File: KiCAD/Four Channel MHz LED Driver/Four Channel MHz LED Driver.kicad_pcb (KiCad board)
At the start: 2 copper layers, 100 x 100 mm, 92 parts, among them J1 Barrel_Jack_Switch, J10 Conn_01x24_Female, J2 Conn_01x02_Female, J3 8P8C_Shielded_x4, J4 Conn_01x03_Male, J5 Conn_01x03_Female, J6 Conn_01x08_Female, J7 Conn_01x03_Female, J8 Conn_01x05_Female, J9 Conn_01x24_Female, M1 Fan_4pin, Q1 SUM70060E, SW1 Pushbutton_with_LED, SW2 Pushbutton_with_LED, SW3 Pushbutton_with_LED, SW4 Pushbutton_with_LED, SW5 SW_SPDT, U1 12V boost, U10 ASSR-1218, U11 ASSR-1218, U12 Teensy3.6, U2 SN74LV4T125PWR, U3 DPBW06F-05, U4 TMUX1204DGSR, U5 BDJ0GA5WEFJ-E2, U6 ADP7182AUJZ-1.8-R7, U7 LT6200CS8-10, U8 ASSR-1218, U9 ASSR-1218

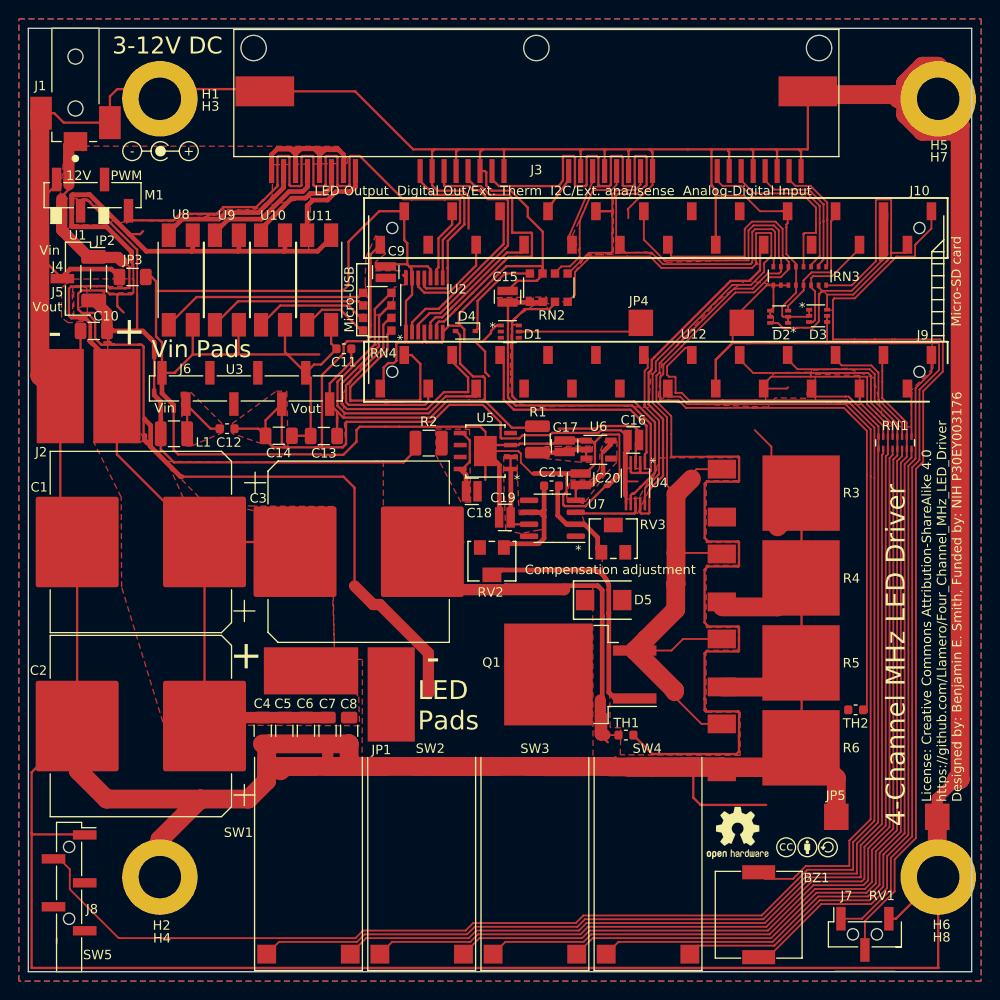
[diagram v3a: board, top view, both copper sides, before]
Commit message: Fix 4.7kx8 footprint
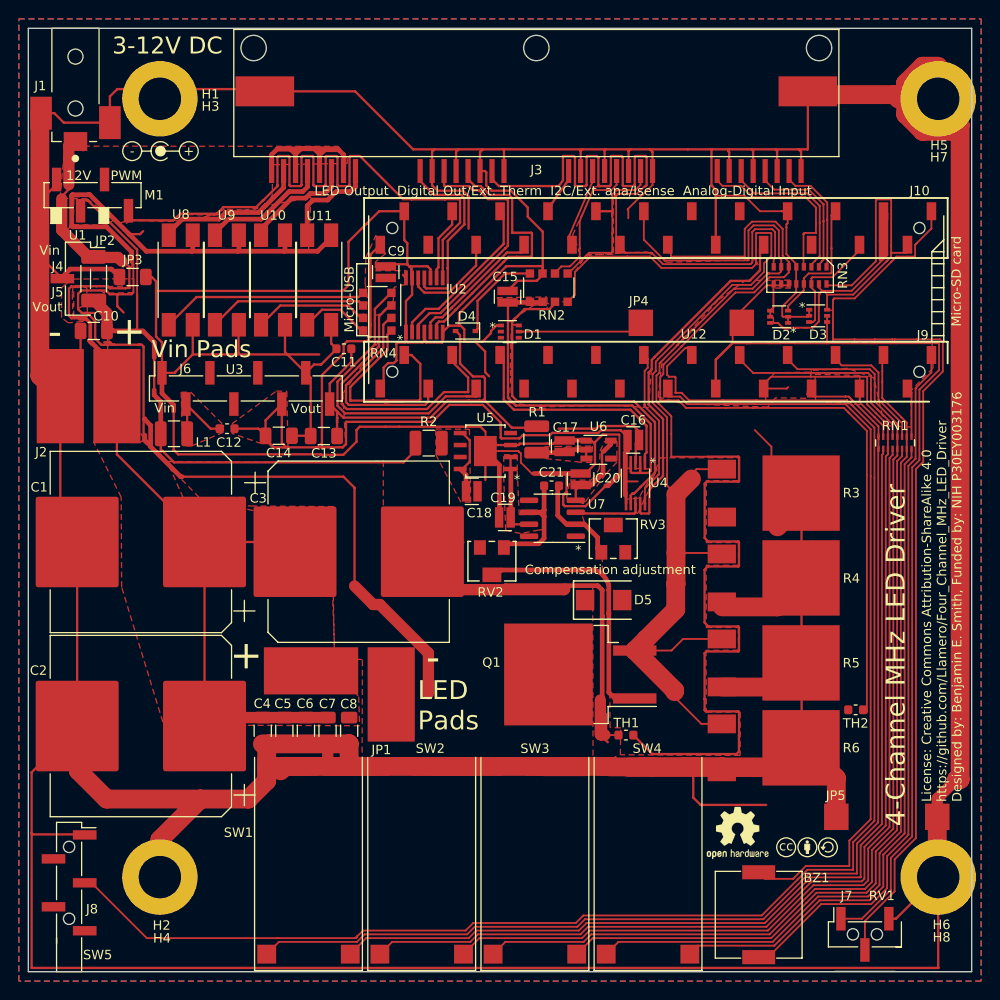
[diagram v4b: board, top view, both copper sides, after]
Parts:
- RN3: footprint Custom Footprints:2506_8x_R-pack -> Custom Footprints:2506_modified_concave_8x_R-pack
- moved R1 0.08 mm to (90.9, 67.6)
- moved RN3 0.07 mm to (118.8, 50.2), turned to 180 degrees
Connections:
- SW5 pad 2: /Toggle_switch -> GND
- SW5 pad 3: Net-(SW5-Pad3) -> /Toggle_switch
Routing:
- net /Toggle_switch: track 170.6 -> 166.0 mm
- net /A-D_input_1: track 13.8 -> 14.9 mm

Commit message: Schematic check
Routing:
- net /Isense: track 117.8 -> 124.5 mm

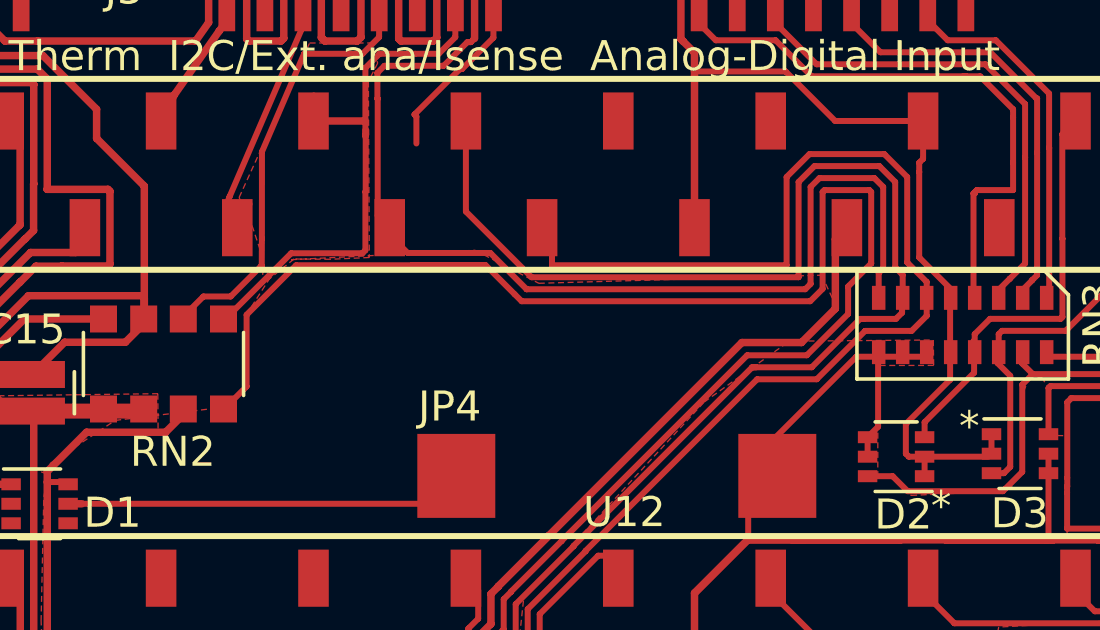
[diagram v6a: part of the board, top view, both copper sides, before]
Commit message: Fix back silkscreen lines
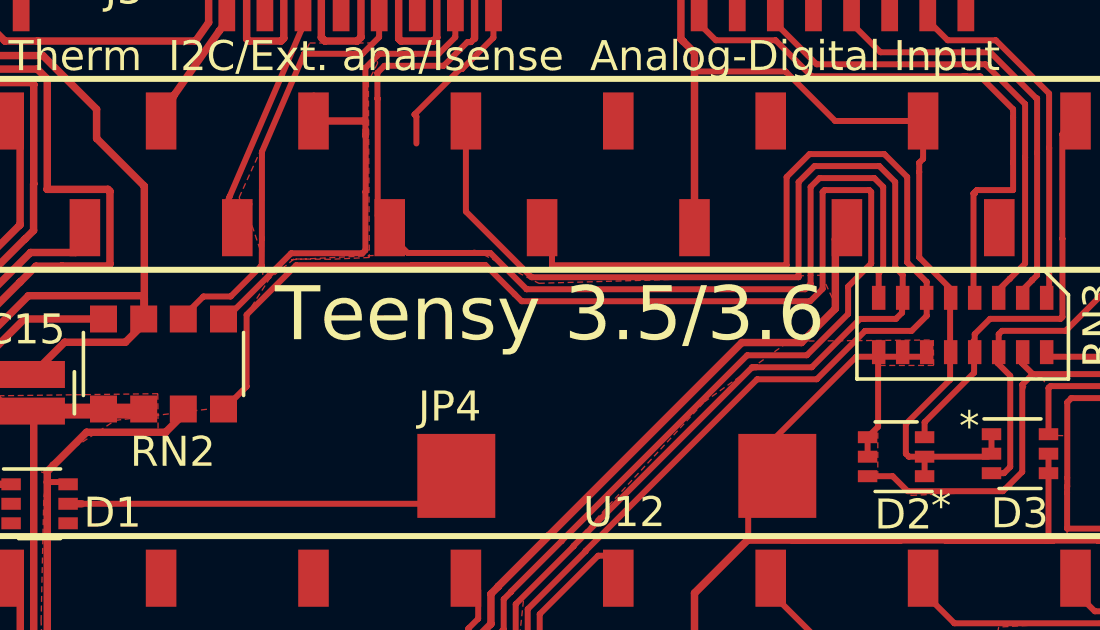
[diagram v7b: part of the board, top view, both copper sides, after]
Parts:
- RN4: value R_Pack04 -> 200
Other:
- board text added: "Teensy 3.5/3.6"
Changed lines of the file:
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@@
   (general
     (thickness 1.6)
-    (drawings 18)
+    (drawings 19)
     (tracks 1938)
     (zones 0)
@@
       (effects (font (size 1 1) (thickness 0.15)))
     )
-    (fp_text value R_Pack04 (at 0 3.5) (layer F.Fab)
+    (fp_text value 200 (at 0 3.5) (layer F.Fab)
       (effects (font (size 1 1) (thickness 0.15)))
     )
@@
     )
   )
-  (gr_line (start 50.99 31.48) (end 133.65 114.04) (layer B.SilkS) (width 0.15))
-  (gr_line (start 133.65 31.5) (end 50.37 114.86) (layer B.SilkS) (width 0.15))
+  (gr_text "Teensy 3.5/3.6" (at 105.05 49.83) (layer F.SilkS)
+    (effects (font (size 1.8 1.8) (thickness 0.3)))
+  )
+  (gr_line (start 88.67 69.15) (end 95.86 76.31) (layer B.SilkS) (width 0.15))
+  (gr_line (start 95.87 69.15) (end 88.68 76.28) (layer B.SilkS) (width 0.15))
   (gr_text * (at 95.31 79.3) (layer F.SilkS)
     (effects (font (size 1 1) (thickness 0.15)))

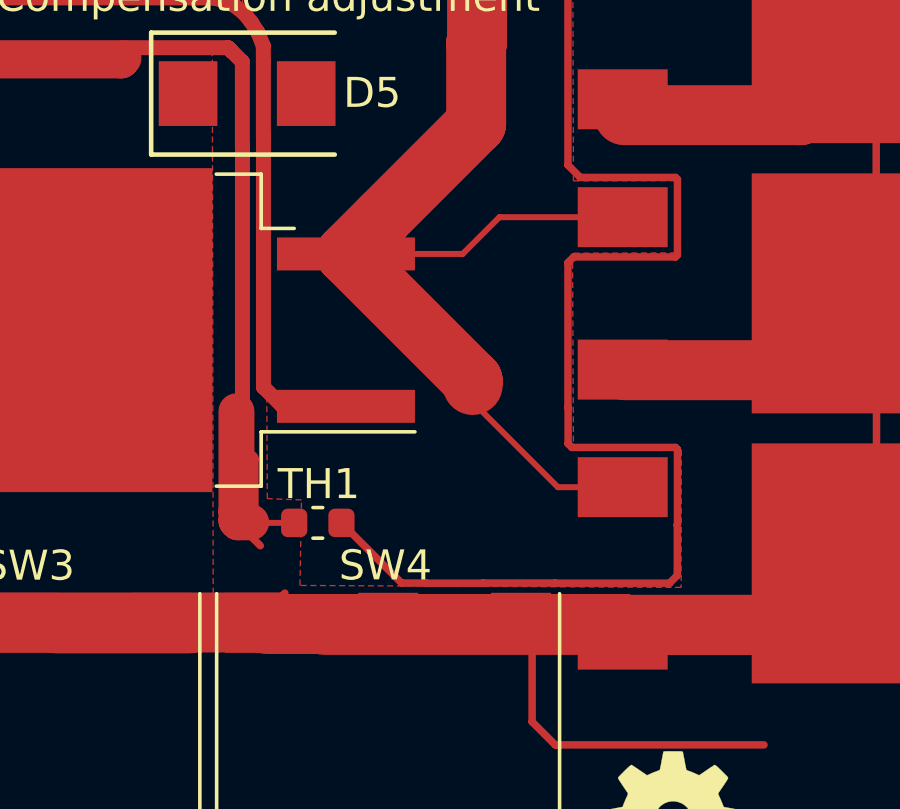
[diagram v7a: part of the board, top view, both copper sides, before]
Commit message: improved thermistor pour
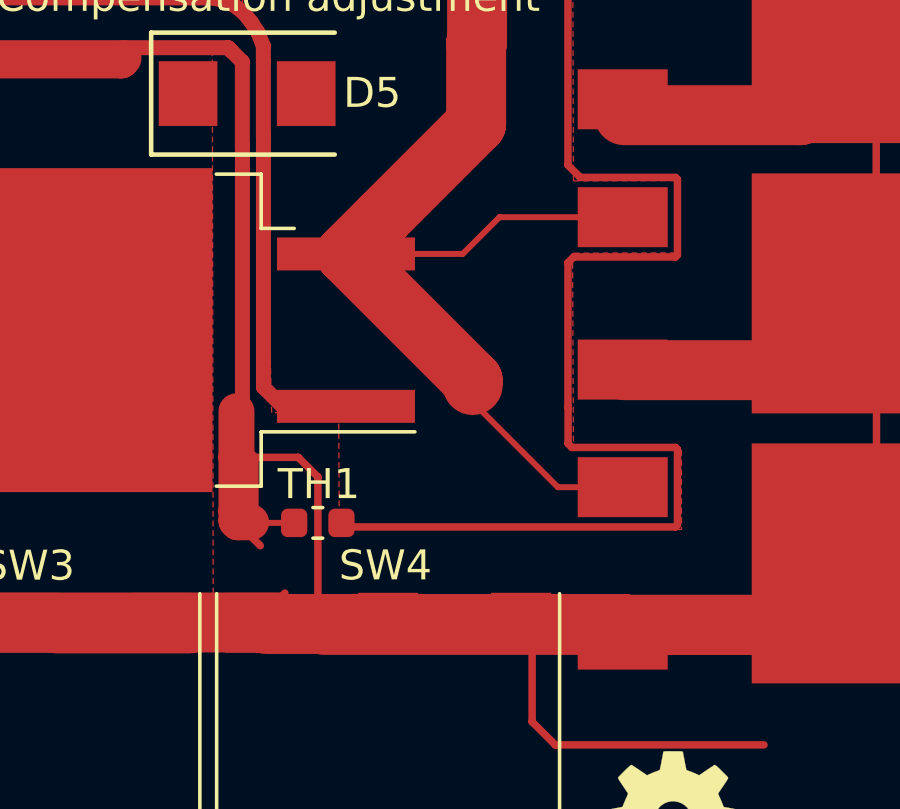
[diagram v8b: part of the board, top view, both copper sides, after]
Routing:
- net GND: track 1178.7 -> 1186.7 mm
- net /MOSFET_temp: track 125.4 -> 122.8 mm
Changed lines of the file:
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@@
     (thickness 1.6)
     (drawings 19)
-    (tracks 1938)
+    (tracks 1935)
     (zones 0)
     (modules 92)
@@
     )
     (pad 2 smd roundrect (at 0.7875 0 180) (size 0.875 0.95) (layers F.Cu F.Paste F.Mask) (roundrect_rratio 0.25)
-      (net 2 GND) (zone_connect 0))
+      (net 2 GND) (zone_connect 1) (thermal_width 0.22) (thermal_gap 0.5))
     (pad 1 smd roundrect (at -0.7875 0 180) (size 0.875 0.95) (layers F.Cu F.Paste F.Mask) (roundrect_rratio 0.25)
       (net 40 /MOSFET_temp) (zone_connect 1))
@@
   (segment (start 98.125 98.9) (end 97.6875 98.9) (width 1.2) (layer F.Cu) (net 2))
   (segment (start 97.6875 98.9) (end 97.635001 98.847501) (width 1.2) (layer F.Cu) (net 2))
-  (segment (start 97.635001 98.535001) (end 97.635001 95.199939) (width 1.2) (layer F.Cu) (net 2))
   (segment (start 98.02 98.92) (end 97.635001 98.535001) (width 0.2) (layer F.Cu) (net 2))
   (segment (start 99.56 98.92) (end 98.02 98.92) (width 0.2) (layer F.Cu) (net 2))
@@
   (segment (start 89.21 70.03) (end 90.37 71.19) (width 0.2) (layer F.Cu) (net 2))
   (segment (start 89.21 69.070898) (end 89.21 70.03) (width 0.2) (layer F.Cu) (net 2))
+  (segment (start 97.635001 96.735001) (end 99.695001 96.735001) (width 0.25) (layer F.Cu) (net 2))
+  (segment (start 97.635001 96.735001) (end 97.635001 95.199939) (width 1.2) (layer F.Cu) (net 2))
+  (segment (start 97.635001 98.535001) (end 97.635001 96.735001) (width 1.2) (layer F.Cu) (net 2))
+  (segment (start 99.695001 96.735001) (end 100.35 97.39) (width 0.25) (layer F.Cu) (net 2))
+  (segment (start 100.35 102.113845) (end 100.556155 102.32) (width 0.25) (layer F.Cu) (net 2))
+  (segment (start 100.35 97.39) (end 100.35 102.113845) (width 0.25) (layer F.Cu) (net 2))
   (segment (start 45.34 54.5) (end 43.92 53.08) (width 0.25) (layer F.Cu) (net 3))
   (segment (start 45.34 56.08) (end 45.34 54.5) (width 0.25) (layer F.Cu) (net 3))
@@
   (segment (start 105.149794 65.119794) (end 105.105592 65.075592) (width 0.2) (layer F.Cu) (net 40))
   (segment (start 103.802899 63.767101) (end 103.807899 63.772101) (width 0.2) (layer F.Cu) (net 40))
-  (segment (start 103.139999 100.924999) (end 101.135 98.92) (width 0.25) (layer F.Cu) (net 40))
-  (segment (start 103.950001 100.924999) (end 103.139999 100.924999) (width 0.25) (layer F.Cu) (net 40))
-  (segment (start 105.859999 100.924999) (end 105.854998 100.93) (width 0.25) (layer F.Cu) (net 40))
-  (segment (start 108.254999 100.924999) (end 105.859999 100.924999) (width 0.25) (layer F.Cu) (net 40))
-  (segment (start 108.26 100.93) (end 108.254999 100.924999) (width 0.25) (layer F.Cu) (net 40))
-  (segment (start 112.07 100.93) (end 108.26 100.93) (width 0.25) (layer F.Cu) (net 40))
-  (segment (start 112.33 100.67) (end 112.07 100.93) (width 0.25) (layer F.Cu) (net 40))
-  (segment (start 103.955002 100.93) (end 103.950001 100.924999) (width 0.25) (layer F.Cu) (net 40))
-  (segment (start 112.33 98.995002) (end 112.33 100.67) (width 0.25) (layer F.Cu) (net 40))
-  (segment (start 112.335001 96.469999) (end 112.335001 98.990001) (width 0.25) (layer F.Cu) (net 40))
   (segment (start 112.270001 96.404999) (end 112.335001 96.469999) (width 0.25) (layer F.Cu) (net 40))
   (segment (start 108.815001 96.404999) (end 112.270001 96.404999) (width 0.25) (layer F.Cu) (net 40))
@@
   (segment (start 109.06 78.394999) (end 112.270001 78.394999) (width 0.25) (layer F.Cu) (net 40))
   (segment (start 109.02 69.404999) (end 112.280001 69.404999) (width 0.25) (layer F.Cu) (net 40))
-  (segment (start 112.335001 98.990001) (end 112.33 98.995002) (width 0.25) (layer F.Cu) (net 40))
   (segment (start 112.280001 69.404999) (end 112.345001 69.469999) (width 0.25) (layer F.Cu) (net 40))
   (segment (start 108.694999 72.285001) (end 108.694999 78.024999) (width 0.25) (layer F.Cu) (net 40))
@@
   (segment (start 108.874999 90.055001) (end 108.684999 90.245001) (width 0.25) (layer F.Cu) (net 40))
   (segment (start 108.684999 81.395001) (end 108.684999 86.994999) (width 0.25) (layer F.Cu) (net 40))
-  (segment (start 105.854998 100.93) (end 103.955002 100.93) (width 0.25) (layer F.Cu) (net 40))
   (segment (start 109.09 87.4) (end 109.09 87.404999) (width 0.25) (layer F.Cu) (net 40))
   (segment (start 112.345001 69.469999) (end 112.345001 71.990001) (width 0.25) (layer F.Cu) (net 40))
@@
   (segment (start 115.39003 49.987777) (end 115.517777 49.987777) (width 0.2) (layer F.Cu) (net 40))
   (segment (start 115.517777 49.987777) (end 115.517779 49.987779) (width 0.2) (layer F.Cu) (net 40))
+  (segment (start 101.270001 99.055001) (end 101.135 98.92) (width 0.25) (layer F.Cu) (net 40))
+  (segment (start 112.270001 99.055001) (end 101.270001 99.055001) (width 0.25) (layer F.Cu) (net 40))
+  (segment (start 112.335001 96.469999) (end 112.335001 98.990001) (width 0.25) (layer F.Cu) (net 40))
+  (segment (start 112.335001 98.990001) (end 112.270001 99.055001) (width 0.25) (layer F.Cu) (net 40))
   (segment (start 125.68 121.695) (end 125.68 122.52) (width 0.25) (layer F.Cu) (net 41))
   (segment (start 132.73 45.222602) (end 132.73 43.39) (width 0.2) (layer F.Cu) (net 41))
@@
         (xy 103.947737 69.530402) (xy 112.297737 69.520402) (xy 112.287737 71.950402) (xy 108.867737 71.940402) (xy 108.857737 78.510402)
         (xy 112.277737 78.510402) (xy 112.287737 80.920402) (xy 108.847737 80.920402) (xy 108.867737 87.520402) (xy 112.267737 87.510402)
-        (xy 112.277737 89.920402) (xy 108.837737 89.930402) (xy 108.867737 96.490402) (xy 112.462737 96.495402) (xy 112.457737 101.070402)
-        (xy 99.752737 101.005402) (xy 99.802737 98.155402) (xy 98.662737 98.110402) (xy 98.612737 87.490402) (xy 98.62 83.14)
+        (xy 112.277737 89.920402) (xy 108.837737 89.930402) (xy 108.867737 96.490402) (xy 112.462737 96.495402) (xy 112.47125 99.13625)
+        (xy 101.06 99.01) (xy 101.043497 95.252913) (xy 98.808437 95.247576) (xy 98.612737 87.490402) (xy 98.62 83.14)
         (xy 97.84 81.6) (xy 97.847737 80.090402) (xy 97.437737 78.150402) (xy 95.927737 76.340402) (xy 95.637737 75.390402)
         (xy 100.467737 75.490402) (xy 101.577737 75.430402) (xy 102.877737 72.790402)
